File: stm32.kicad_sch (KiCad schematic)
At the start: 12 parts, among them SW3 SW_Push, U6 STM32G431RBIx, U7 STM32F030F4Px

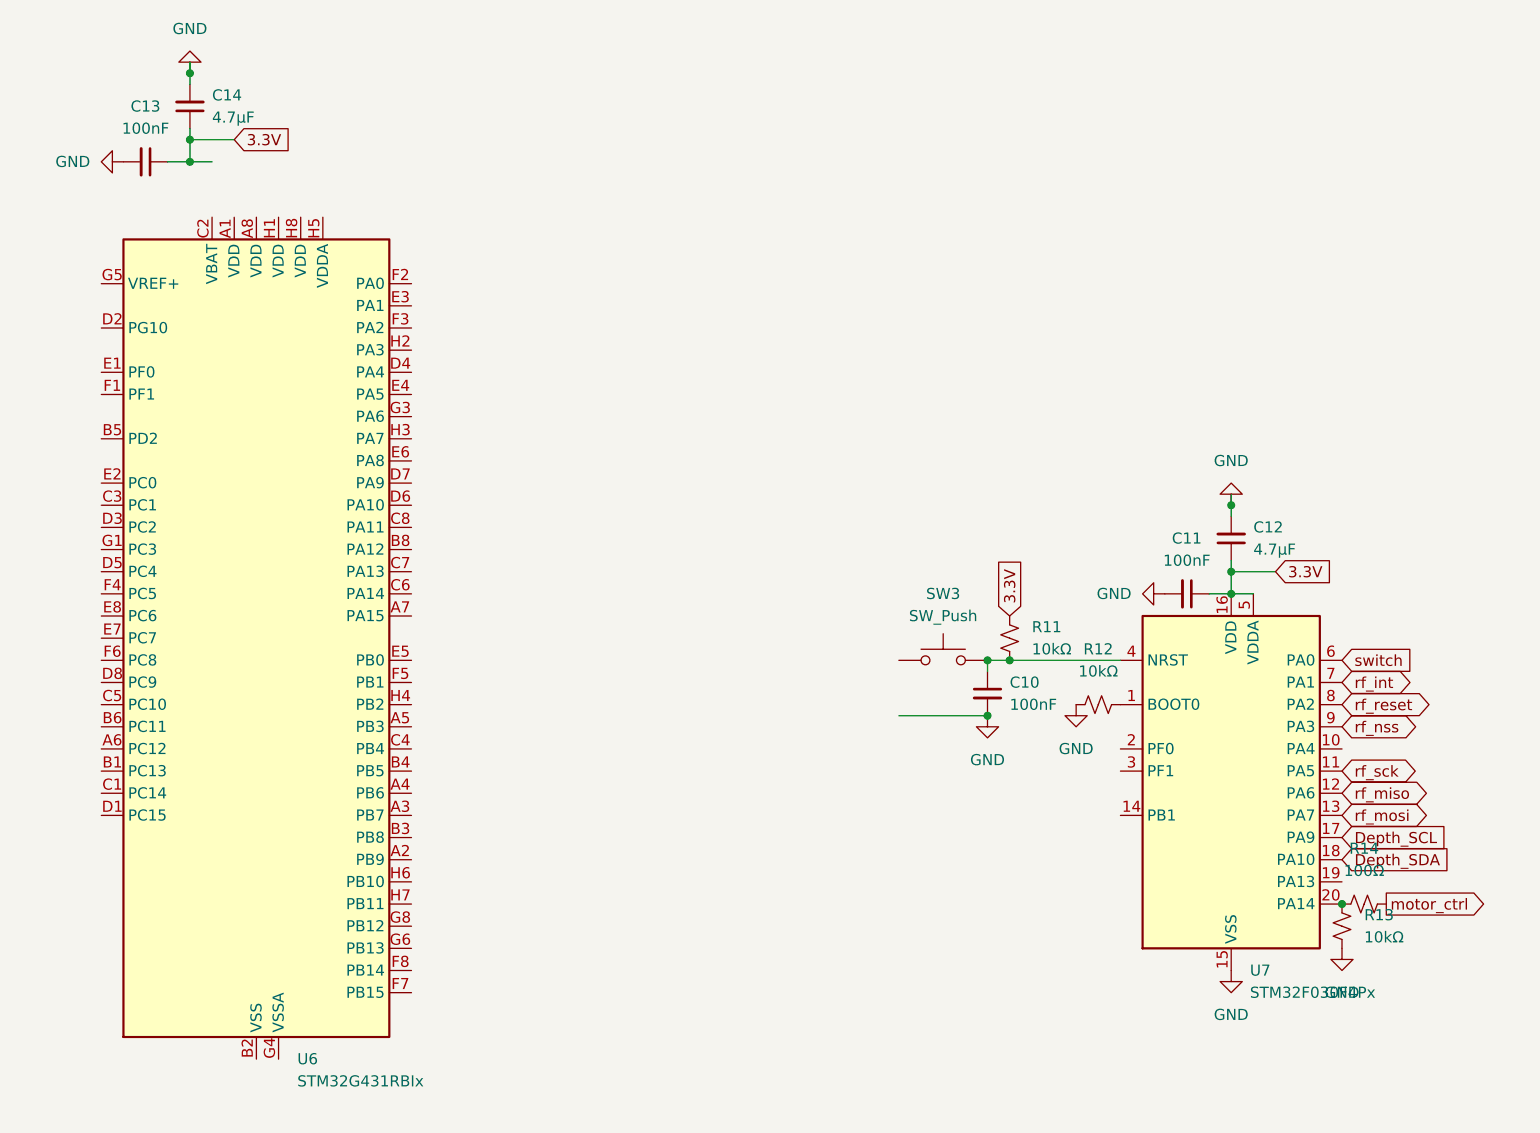
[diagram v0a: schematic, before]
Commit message: Overhaul
Overhauled the schematic so all the components are correct, rewired power to be 12 V instead of 9 V and connected hierarchical labels between modules. Added more decoupling capacitors where they were missing.
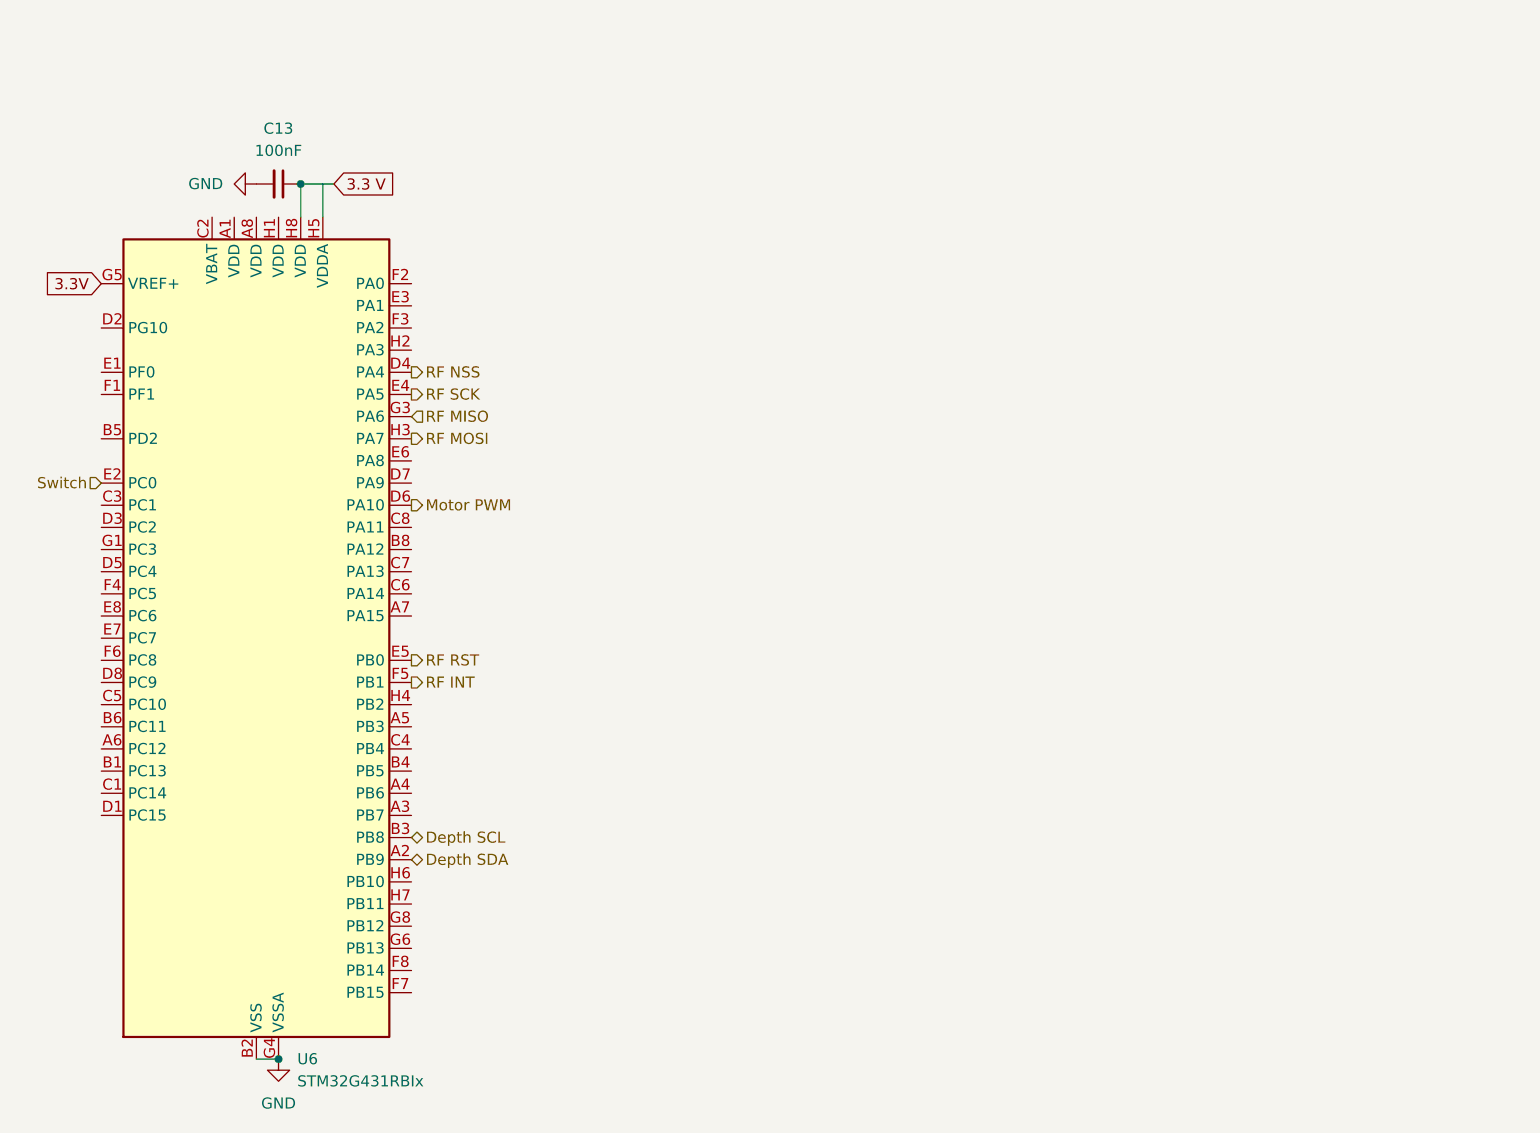
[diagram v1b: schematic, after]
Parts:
- removed C10, C11: 100nF, symbol Device:C_Small
- removed C12, C14: 4.7µF, symbol Device:C_Small
- removed R11, R12, R13: 10kΩ, symbol Device:R_Small_US
- removed R14: 100Ω, symbol Device:R_Small_US
- removed SW3: SW_Push, symbol Switch:SW_Push
- removed U7: STM32F030F4Px, Package_SO:TSSOP-20_4.4x6.5mm_P0.65mm, symbol MCU_ST_STM32F0:STM32F030F4Px
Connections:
- net 3.3V: now also U6.G5 (VREF+); no longer C13.1
- net GND: now also U6.B2 (VSS), U6.B7 (VSS), U6.G2 (VSS), U6.G4 (VSSA), U6.G7 (VSS)
- net Depth SDA: now reaches U6.A2 (PB9)
- net Depth SCL: now reaches U6.B3 (PB8)
- net RF NSS: now reaches U6.D4 (PA4)
- net Motor PWM: now reaches U6.D6 (PA10)
- net Switch: now reaches U6.E2 (PC0)
- net RF SCK: now reaches U6.E4 (PA5)
- net RF RST: now reaches U6.E5 (PB0)
- net RF INT: now reaches U6.F5 (PB1)
- net RF MISO: now reaches U6.G3 (PA6)
- net RF MOSI: now reaches U6.H3 (PA7)
- net 3.3 V: now reaches U6.H8 (VDD)
- net 3.3 V: now also C13.1
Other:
- moved on the sheet: C13

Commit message: Clean up
Minor fixes to mistakes in the schematic
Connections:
- net 3.3 V: now also U6.H5 (VDDA)
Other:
- moved on the sheet: C13, U6
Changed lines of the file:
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@@
 	(paper "A4")
 	(junction
-		(at 55.88 29.21)
+		(at 46.99 19.05)
 		(diameter 0)
 		(color 0 0 0 0)
 	)
 	(junction
-		(at 53.34 129.54)
+		(at 44.45 19.05)
 		(diameter 0)
 		(color 0 0 0 0)
 	)
+	(junction
+		(at 41.91 119.38)
+		(diameter 0)
+		(color 0 0 0 0)
+	)
 	(wire
 		(pts
-			(xy 55.88 29.21) (xy 55.88 33.02)
+			(xy 44.45 19.05) (xy 44.45 22.86)
 		)
 		(stroke
@@
 	(wire
 		(pts
-			(xy 55.88 29.21) (xy 59.69 29.21)
+			(xy 46.99 19.05) (xy 48.26 19.05)
 		)
 		(stroke
@@
 	(wire
 		(pts
-			(xy 58.42 29.21) (xy 58.42 33.02)
+			(xy 44.45 19.05) (xy 46.99 19.05)
 		)
 		(stroke
@@
 	(wire
 		(pts
-			(xy 50.8 129.54) (xy 53.34 129.54)
+			(xy 46.99 19.05) (xy 46.99 22.86)
 		)
 		(stroke
@@
 		)
 	)
+	(wire
+		(pts
+			(xy 39.37 119.38) (xy 41.91 119.38)
+		)
+		(stroke
+			(width 0)
+			(type default)
+		)
+	)
 	(global_label "3.3V"
 		(shape input)
-		(at 33.02 40.64 180)
+		(at 21.59 30.48 180)
 		(fields_autoplaced yes)
 		(effects
@@
 		)
 		(property "Intersheetrefs" "${INTERSHEET_REFS}"
-			(at 25.9224 40.64 0)
+			(at 14.4924 30.48 0)
 			(hide yes)
 			(show_name no)
@@
 	(global_label "3.3 V"
 		(shape input)
-		(at 59.69 29.21 0)
+		(at 48.26 19.05 0)
 		(fields_autoplaced yes)
 		(effects
@@
 		)
 		(property "Intersheetrefs" "${INTERSHEET_REFS}"
-			(at 67.7552 29.21 0)
+			(at 56.3252 19.05 0)
 			(hide yes)
 			(show_name no)
@@
 	(hierarchical_label "RF INT"
 		(shape output)
-		(at 68.58 86.36 0)
+		(at 57.15 76.2 0)
 		(effects
 			(font
@@
 	(hierarchical_label "Motor PWM"
 		(shape output)
-		(at 68.58 66.04 0)
+		(at 57.15 55.88 0)
 		(effects
 			(font
@@
 	(hierarchical_label "Depth SCL"
 		(shape bidirectional)
-		(at 68.58 104.14 0)
+		(at 57.15 93.98 0)
 		(effects
 			(font
@@
 	(hierarchical_label "RF RST"
 		(shape output)
-		(at 68.58 83.82 0)
+		(at 57.15 73.66 0)
 		(effects
 			(font
@@
 	(hierarchical_label "Switch"
 		(shape input)
-		(at 33.02 63.5 180)
+		(at 21.59 53.34 180)
 		(effects
 			(font
@@
 	(hierarchical_label "RF MISO"
 		(shape input)
-		(at 68.58 55.88 0)
+		(at 57.15 45.72 0)
 		(effects
 			(font
@@
 	(hierarchical_label "Depth SDA"
 		(shape bidirectional)
-		(at 68.58 106.68 0)
+		(at 57.15 96.52 0)
 		(effects
 			(font
@@
 	(hierarchical_label "RF SCK"
 		(shape output)
-		(at 68.58 53.34 0)
+		(at 57.15 43.18 0)
 		(effects
 			(font
@@
 	(hierarchical_label "RF NSS"
 		(shape output)
-		(at 68.58 50.8 0)
+		(at 57.15 40.64 0)
 		(effects
 			(font
@@
 	(hierarchical_label "RF MOSI"
 		(shape output)
-		(at 68.58 58.42 0)
+		(at 57.15 48.26 0)
 		(effects
 			(font
@@
 	(symbol
 		(lib_id "MCU_ST_STM32G4:STM32G431RBIx")
-		(at 50.8 81.28 0)
+		(at 39.37 71.12 0)
 		(unit 1)
 		(body_style 1)
@@
 		(fields_autoplaced yes)
 		(property "Reference" "U6"
-			(at 55.4833 129.54 0)
+			(at 44.0533 119.38 0)
 			(show_name no)
 			(do_not_autoplace no)
@@
 		)
 		(property "Value" "STM32G431RBIx"
-			(at 55.4833 132.08 0)
+			(at 44.0533 121.92 0)
 			(show_name no)
 			(do_not_autoplace no)
@@
 		)
 		(property "Footprint" "Package_BGA:UFBGA-64_5x5mm_Layout8x8_P0.5mm"
-			(at 35.56 127 0)
+			(at 24.13 116.84 0)
 			(hide yes)
 			(show_name no)
@@
 		)
 		(property "Datasheet" "https://www.st.com/resource/en/datasheet/stm32g431rb.pdf"
-			(at 50.8 81.28 0)
+			(at 39.37 71.12 0)
 			(hide yes)
 			(show_name no)
@@
 		)
 		(property "Description" "STMicroelectronics Arm Cortex-M4 MCU, 128KB flash, 32KB RAM, 170 MHz, 1.71-3.6V, 52 GPIO, UFBGA64"
-			(at 50.8 81.28 0)
+			(at 39.37 71.12 0)
 			(hide yes)
 			(show_name no)
@@
 	(symbol
 		(lib_id "Device:C_Small")
-		(at 53.34 29.21 270)
+		(at 41.91 19.05 270)
 		(unit 1)
 		(body_style 1)
@@
 		(fields_autoplaced yes)
 		(property "Reference" "C13"
-			(at 53.3336 22.86 90)
+			(at 41.9036 12.7 90)
 			(show_name no)
 			(do_not_autoplace no)
@@
 		)
 		(property "Value" "100nF"
-			(at 53.3336 25.4 90)
+			(at 41.9036 15.24 90)
 			(show_name no)
 			(do_not_autoplace no)
@@
 		)
 		(property "Footprint" ""
-			(at 53.34 29.21 0)
+			(at 41.91 19.05 0)
 			(hide yes)
 			(show_name no)
@@
 		)
 		(property "Datasheet" ""
-			(at 53.34 29.21 0)
+			(at 41.91 19.05 0)
 			(hide yes)
 			(show_name no)
@@
 		)
 		(property "Description" "Unpolarized capacitor, small symbol"
-			(at 53.34 29.21 0)
+			(at 41.91 19.05 0)
 			(hide yes)
 			(show_name no)
@@
 	(symbol
 		(lib_id "power:GND")
-		(at 53.34 129.54 0)
+		(at 41.91 119.38 0)
 		(unit 1)
 		(body_style 1)
@@
 		(fields_autoplaced yes)
 		(property "Reference" "#PWR023"
-			(at 53.34 135.89 0)
+			(at 41.91 125.73 0)
 			(hide yes)
 			(show_name no)
@@
 		)
 		(property "Value" "GND"
-			(at 53.34 134.62 0)
+			(at 41.91 124.46 0)
 			(show_name no)
 			(do_not_autoplace no)
@@
 		)
 		(property "Footprint" ""
-			(at 53.34 129.54 0)
+			(at 41.91 119.38 0)
 			(hide yes)
 			(show_name no)
@@
 		)
 		(property "Datasheet" ""
-			(at 53.34 129.54 0)
+			(at 41.91 119.38 0)
 			(hide yes)
 			(show_name no)
@@
 		)
 		(property "Description" "Power symbol creates a global label with name \"GND\" , ground"
-			(at 53.34 129.54 0)
+			(at 41.91 119.38 0)
 			(hide yes)
 			(show_name no)
@@
 	(symbol
 		(lib_id "power:GND")
-		(at 50.8 29.21 270)
+		(at 39.37 19.05 270)
 		(unit 1)
 		(body_style 1)
@@
 		(fields_autoplaced yes)
 		(property "Reference" "#PWR022"
-			(at 44.45 29.21 0)
+			(at 33.02 19.05 0)
 			(hide yes)
 			(show_name no)
@@
 		)
 		(property "Value" "GND"
-			(at 46.99 29.2099 90)
+			(at 35.56 19.0499 90)
 			(show_name no)
 			(do_not_autoplace no)
@@
 		)
 		(property "Footprint" ""
-			(at 50.8 29.21 0)
+			(at 39.37 19.05 0)
 			(hide yes)
 			(show_name no)
@@
 		)
 		(property "Datasheet" ""
-			(at 50.8 29.21 0)
+			(at 39.37 19.05 0)
 			(hide yes)
 			(show_name no)
@@
 		)
 		(property "Description" "Power symbol creates a global label with name \"GND\" , ground"
-			(at 50.8 29.21 0)
-			(hide yes)
-			(show_name no)
+			(at 39.37 19.05 0)
+			(hide yes)
+			(show_name no)

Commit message: Gave footprints to everything
Footprints
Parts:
- C13: footprint (none) -> Capacitor_SMD:C_0603_1608Metric
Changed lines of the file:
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@@
 			)
 		)
-		(property "Footprint" ""
+		(property "Footprint" "Capacitor_SMD:C_0603_1608Metric"
 			(at 41.91 19.05 0)
 			(hide yes)
